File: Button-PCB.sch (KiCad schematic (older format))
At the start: 32 parts

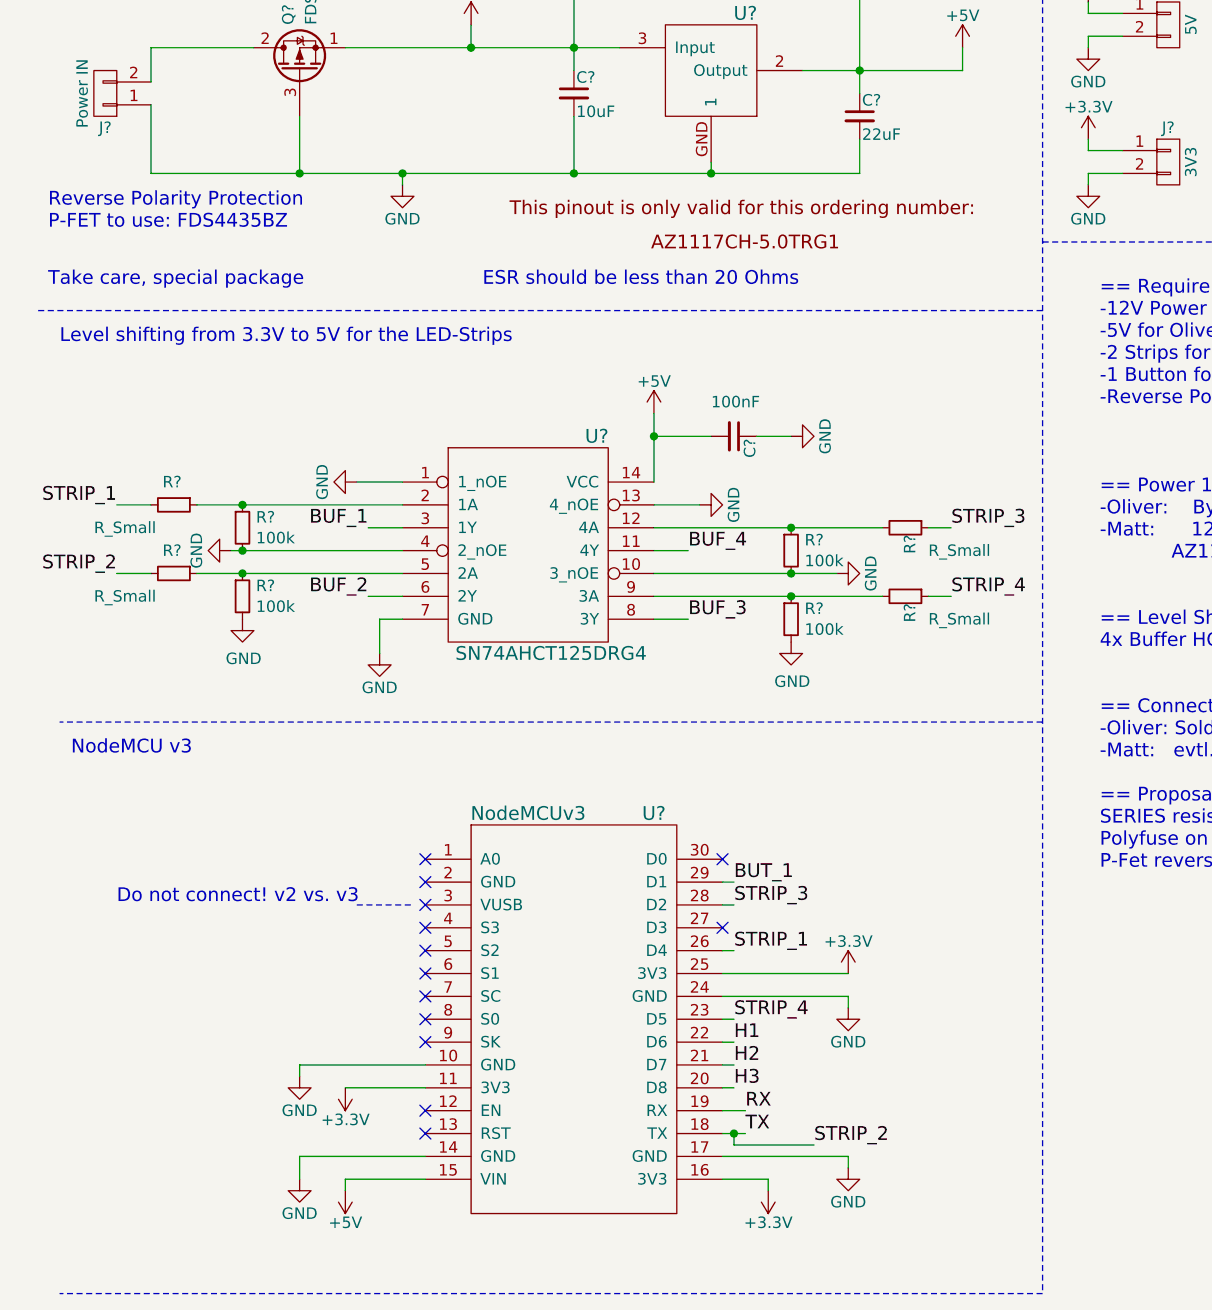
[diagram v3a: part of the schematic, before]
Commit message: Moving series termination resistors from sink (buf) to source (esp)
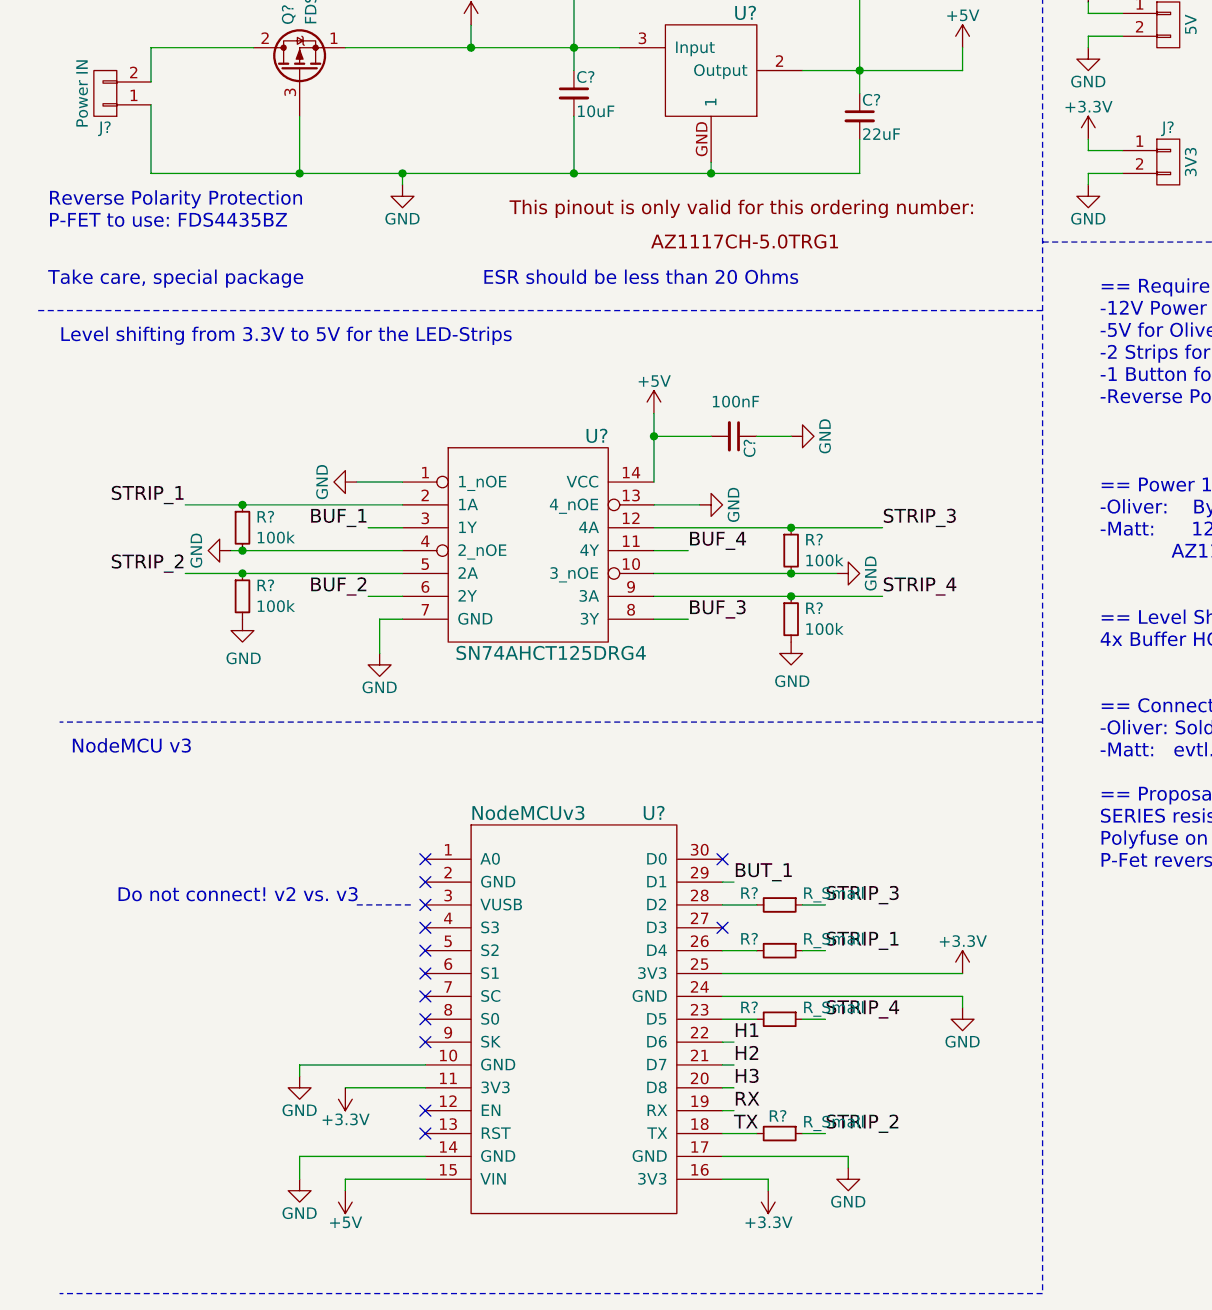
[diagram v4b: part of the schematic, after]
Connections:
- net STRIP_1: now also R?.1, R?.1, U?.2 (1A); no longer R?.2, U?.26 (D4)
- net STRIP_2: now also R?.1, R?.1, U?.5 (2A); no longer J?.1 (P1), R?.2, U?.18 (TX)
- net STRIP_3: now also R?.1, U?.12 (4A); no longer U?.28 (D2)
- net STRIP_4: now also R?.1, U?.9 (3A); no longer U?.23 (D5)
- new net: R?.2, U?.23 (D5)
- new net: R?.2, U?.26 (D4)
- new net: R?.2, U?.28 (D2)
- new net TX: J?.1 (P1), R?.2, U?.18 (TX)
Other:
- moved on the sheet: R?
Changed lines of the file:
@@
 L GND #PWR?
 U 1 1 593F0F99
-P 4050 5850
-F 0 "#PWR?" H 4050 5600 50  0001 C CNN
-F 1 "GND" H 4050 5700 50  0000 C CNN
-F 2 "" H 4050 5850 50  0001 C CNN
-F 3 "" H 4050 5850 50  0001 C CNN
-	1    4050 5850
-	1    0    0    -1
-$EndComp
-Wire Wire Line
-	3500 5800 4050 5800
-Wire Wire Line
-	4050 5800 4050 5850
+P 4550 5850
+F 0 "#PWR?" H 4550 5600 50  0001 C CNN
+F 1 "GND" H 4550 5700 50  0000 C CNN
+F 2 "" H 4550 5850 50  0001 C CNN
+F 3 "" H 4550 5850 50  0001 C CNN
+	1    4550 5850
+	1    0    0    -1
+$EndComp
+Wire Wire Line
+	3500 5800 4550 5800
+Wire Wire Line
+	4550 5800 4550 5850
 Wire Wire Line
 	2200 6100 1650 6100
@@
 L +3.3V #PWR?
 U 1 1 593F1158
-P 4050 5700
-F 0 "#PWR?" H 4050 5550 50  0001 C CNN
-F 1 "+3.3V" H 4050 5840 50  0000 C CNN
-F 2 "" H 4050 5700 50  0001 C CNN
-F 3 "" H 4050 5700 50  0001 C CNN
-	1    4050 5700
+P 4550 5700
+F 0 "#PWR?" H 4550 5550 50  0001 C CNN
+F 1 "+3.3V" H 4550 5840 50  0000 C CNN
+F 2 "" H 4550 5700 50  0001 C CNN
+F 3 "" H 4550 5700 50  0001 C CNN
+	1    4550 5700
 	1    0    0    -1
 $EndComp
@@
 	3700 6600 3700 6650
 Wire Wire Line
-	3500 5700 4050 5700
+	3500 5700 4550 5700
 NoConn ~ 2200 6400
 NoConn ~ 2200 6300
 NoConn ~ 2200 5400
-Text Label 3550 5600 0    60   ~ 0
+Text Label 3950 5600 0    60   ~ 0
 STRIP_1
 Wire Wire Line
-	3500 5600 3550 5600
+	3500 5600 3650 5600
 Text Label 3550 5300 0    60   ~ 0
 BUT_1
 Wire Wire Line
 	3550 5300 3500 5300
-Text Label 3600 6400 0    60   ~ 0
+Text Label 3550 6400 0    60   ~ 0
 TX
-Text Label 3900 6450 0    60   ~ 0
+Text Label 3950 6400 0    60   ~ 0
 STRIP_2
 Wire Wire Line
-	3500 6400 3550 6400
-Wire Wire Line
-	3550 6400 3600 6400
-Wire Wire Line
-	3550 6400 3550 6450
-Wire Wire Line
-	3550 6450 3900 6450
-Connection ~ 3550 6400
-Text Label 3600 6300 0    60   ~ 0
+	3500 6400 3650 6400
+Text Label 3550 6300 0    60   ~ 0
 RX
-Wire Wire Line
-	3500 6300 3600 6300
-Text Label 3550 5400 0    60   ~ 0
+Text Label 3950 5400 0    60   ~ 0
 STRIP_3
-Text Label 3550 5900 0    60   ~ 0
+Text Label 3950 5900 0    60   ~ 0
 STRIP_4
 Wire Wire Line
-	3500 5400 3550 5400
-Wire Wire Line
-	3500 5900 3550 5900
+	3500 5400 3650 5400
+Wire Wire Line
+	3500 5900 3650 5900
 NoConn ~ 2200 5200
 NoConn ~ 2200 5500
@@
 $EndComp
 Wire Wire Line
-	2100 2250 2100 2200
+	2100 2200 2100 2250
 Wire Wire Line
 	4100 2200 4100 2050
 Wire Wire Line
-	3450 2150 3450 2200
+	3450 2200 3450 2150
 Wire Wire Line
 	3850 1750 4100 1750
@@
 	0    -1   -1   0
 $EndComp
-Text Label 850  3950 2    60   ~ 0
+Text Label 1150 3950 2    60   ~ 0
 STRIP_2
-Text Label 850  3650 2    60   ~ 0
+Text Label 1150 3650 2    60   ~ 0
 STRIP_1
-Text Label 4500 3750 0    60   ~ 0
+Text Label 4200 3750 0    60   ~ 0
 STRIP_3
-Text Label 4500 4050 0    60   ~ 0
+Text Label 4200 4050 0    60   ~ 0
 STRIP_4
 $Comp
 L R_Small R?
 U 1 1 5942C75E
-P 1100 3650
-F 0 "R?" V 1000 3600 50  0000 L CNN
-F 1 "R_Small" V 1200 3300 50  0000 L CNN
-F 2 "" H 1100 3650 50  0001 C CNN
-F 3 "" H 1100 3650 50  0001 C CNN
-	1    1100 3650
+P 3750 5600
+F 0 "R?" V 3700 5425 50  0000 L CNN
+F 1 "R_Small" V 3700 5700 50  0000 L CNN
+F 2 "" H 3750 5600 50  0001 C CNN
+F 3 "" H 3750 5600 50  0001 C CNN
+	1    3750 5600
 	0    1    1    0
 $EndComp
@@
 L R_Small R?
 U 1 1 5942CA98
-P 1100 3950
-F 0 "R?" V 1000 3900 50  0000 L CNN
-F 1 "R_Small" V 1200 3600 50  0000 L CNN
-F 2 "" H 1100 3950 50  0001 C CNN
-F 3 "" H 1100 3950 50  0001 C CNN
-	1    1100 3950
+P 3750 6400
+F 0 "R?" V 3675 6350 50  0000 L CNN
+F 1 "R_Small" V 3700 6500 50  0000 L CNN
+F 2 "" H 3750 6400 50  0001 C CNN
+F 3 "" H 3750 6400 50  0001 C CNN
+	1    3750 6400
 	0    1    1    0
 $EndComp
@@
 	1950 3750 2100 3750
 Wire Wire Line
-	1200 3650 1400 3650
+	1150 3650 1400 3650
 Wire Wire Line
 	1400 3650 2100 3650
 Wire Wire Line
-	1200 3950 1400 3950
+	1150 3950 1400 3950
 Wire Wire Line
 	1400 3950 2100 3950
@@
 	1900 3550 2100 3550
 Wire Wire Line
-	4000 3950 3800 3950
-Wire Wire Line
-	3800 3950 3200 3950
+	3200 3950 3800 3950
+Wire Wire Line
+	3800 3950 4000 3950
 Wire Wire Line
 	3400 3650 3200 3650
@@
 L R_Small R?
 U 1 1 5942EF55
-P 4300 3750
-F 0 "R?" H 4330 3770 50  0000 L CNN
-F 1 "R_Small" V 4400 3850 50  0000 L CNN
-F 2 "" H 4300 3750 50  0001 C CNN
-F 3 "" H 4300 3750 50  0001 C CNN
-	1    4300 3750
+P 3750 5400
+F 0 "R?" V 3700 5225 50  0000 L CNN
+F 1 "R_Small" V 3700 5500 50  0000 L CNN
+F 2 "" H 3750 5400 50  0001 C CNN
+F 3 "" H 3750 5400 50  0001 C CNN
+	1    3750 5400
 	0    1    1    0
 $EndComp
@@
 L R_Small R?
 U 1 1 5942F05B
-P 4300 4050
-F 0 "R?" H 4330 4070 50  0000 L CNN
-F 1 "R_Small" V 4400 4150 50  0000 L CNN
-F 2 "" H 4300 4050 50  0001 C CNN
-F 3 "" H 4300 4050 50  0001 C CNN
-	1    4300 4050
+P 3750 5900
+F 0 "R?" V 3700 5725 50  0000 L CNN
+F 1 "R_Small" V 3700 6000 50  0000 L CNN
+F 2 "" H 3750 5900 50  0001 C CNN
+F 3 "" H 3750 5900 50  0001 C CNN
+	1    3750 5900
 	0    1    1    0
 $EndComp
@@
 Wire Wire Line
 	3800 4050 4200 4050
-Wire Wire Line
-	4400 3750 4500 3750
-Wire Wire Line
-	4500 4050 4400 4050
 $Comp
 L C_Small C?
@@
 Wire Notes Line
 	4900 7100 600  7100
-Wire Wire Line
-	1000 3650 850  3650
-Wire Wire Line
-	1000 3950 850  3950
 $Comp
 L R_Small R?
@@
 $EndComp
 Connection ~ 3800 3950
+Wire Wire Line
+	3950 5600 3850 5600
+Wire Wire Line
+	3850 5900 3950 5900
+Wire Wire Line
+	3550 6300 3500 6300
+Wire Wire Line
+	3850 6400 3950 6400
+Wire Wire Line
+	3950 5400 3850 5400
 $EndSCHEMATC

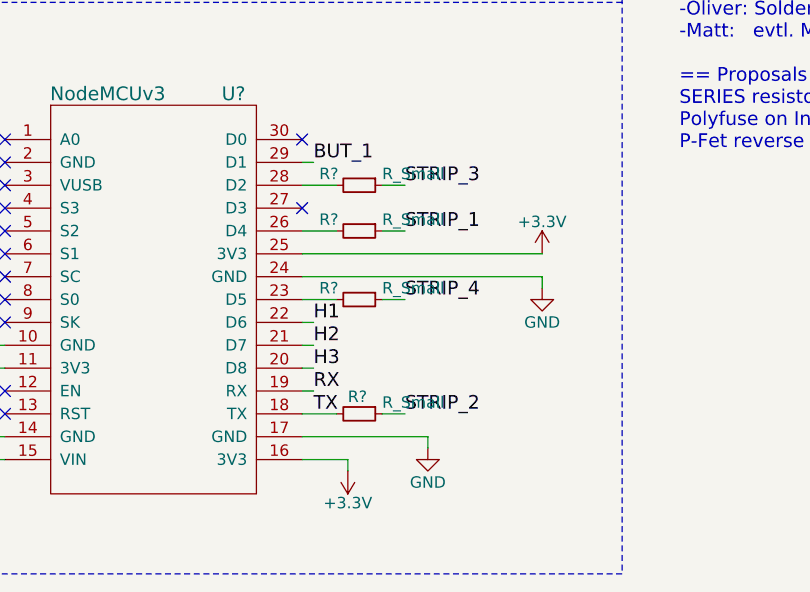
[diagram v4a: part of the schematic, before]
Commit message: Value of series termination resistors: 100R
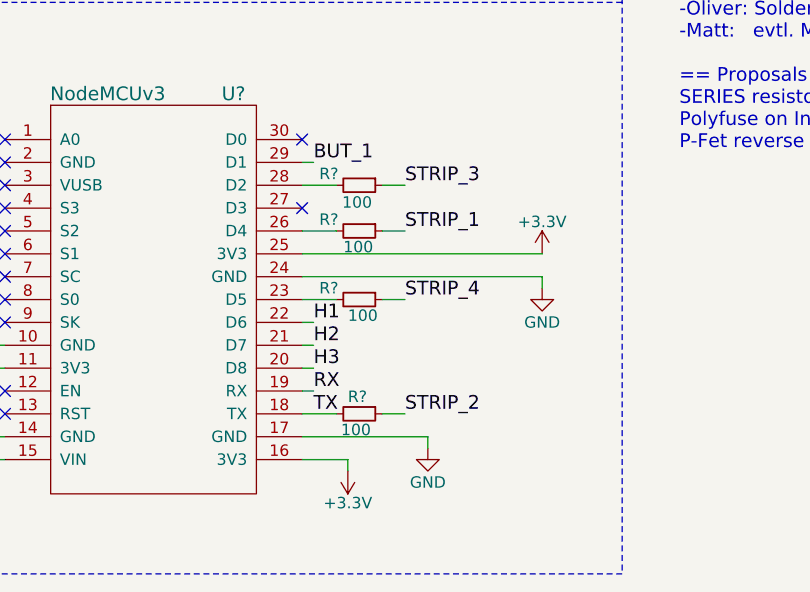
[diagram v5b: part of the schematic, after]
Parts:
- R? (x4): value R_Small -> 100
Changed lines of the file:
@@
 P 3750 5600
 F 0 "R?" V 3700 5425 50  0000 L CNN
-F 1 "R_Small" V 3700 5700 50  0000 L CNN
+F 1 "100" V 3820 5530 50  0000 L CNN
 F 2 "" H 3750 5600 50  0001 C CNN
 F 3 "" H 3750 5600 50  0001 C CNN
@@
 P 3750 6400
 F 0 "R?" V 3675 6350 50  0000 L CNN
-F 1 "R_Small" V 3700 6500 50  0000 L CNN
+F 1 "100" V 3820 6320 50  0000 L CNN
 F 2 "" H 3750 6400 50  0001 C CNN
 F 3 "" H 3750 6400 50  0001 C CNN
@@
 P 3750 5400
 F 0 "R?" V 3700 5225 50  0000 L CNN
-F 1 "R_Small" V 3700 5500 50  0000 L CNN
+F 1 "100" V 3825 5325 50  0000 L CNN
 F 2 "" H 3750 5400 50  0001 C CNN
 F 3 "" H 3750 5400 50  0001 C CNN
@@
 P 3750 5900
 F 0 "R?" V 3700 5725 50  0000 L CNN
-F 1 "R_Small" V 3700 6000 50  0000 L CNN
+F 1 "100" V 3820 5850 50  0000 L CNN
 F 2 "" H 3750 5900 50  0001 C CNN
 F 3 "" H 3750 5900 50  0001 C CNN

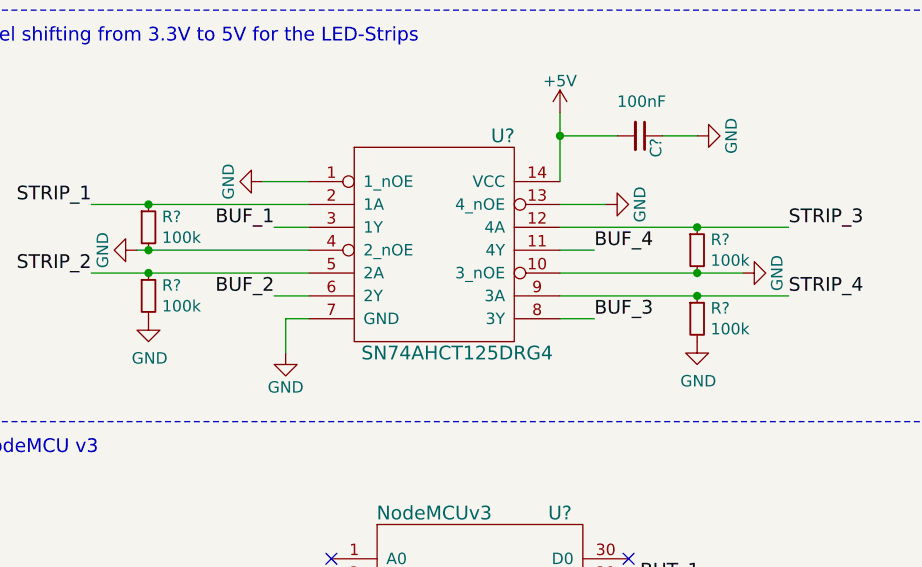
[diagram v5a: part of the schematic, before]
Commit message: Reducing pull-down resistor values from 100k to 10k
A 10k resistor is already used as pull-up for the button. This change
keeps the number of distinct resistor values low.
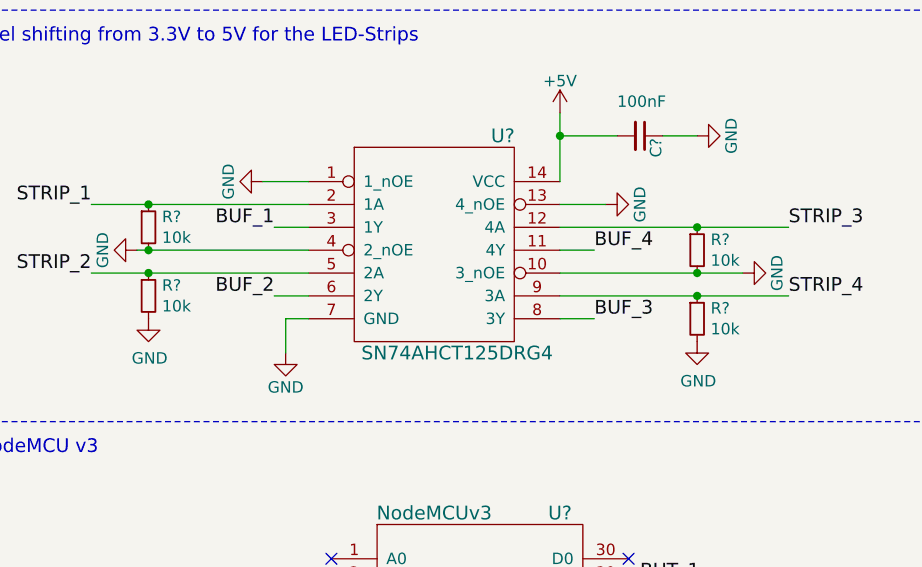
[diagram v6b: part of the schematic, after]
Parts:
- R? (x4): value 100k -> 10k
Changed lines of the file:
@@
 P 1400 4050
 F 0 "R?" H 1459 4096 50  0000 L CNN
-F 1 "100k" H 1459 4005 50  0000 L CNN
+F 1 "10k" H 1459 4005 50  0000 L CNN
 F 2 "" H 1400 4050 50  0001 C CNN
 F 3 "" H 1400 4050 50  0001 C CNN
@@
 P 1400 3750
 F 0 "R?" H 1459 3796 50  0000 L CNN
-F 1 "100k" H 1459 3705 50  0000 L CNN
+F 1 "10k" H 1459 3705 50  0000 L CNN
 F 2 "" H 1400 3750 50  0001 C CNN
 F 3 "" H 1400 3750 50  0001 C CNN
@@
 P 3800 3850
 F 0 "R?" H 3859 3896 50  0000 L CNN
-F 1 "100k" H 3859 3805 50  0000 L CNN
+F 1 "10k" H 3859 3805 50  0000 L CNN
 F 2 "" H 3800 3850 50  0001 C CNN
 F 3 "" H 3800 3850 50  0001 C CNN
@@
 P 3800 4150
 F 0 "R?" H 3859 4196 50  0000 L CNN
-F 1 "100k" H 3859 4105 50  0000 L CNN
+F 1 "10k" H 3859 4105 50  0000 L CNN
 F 2 "" H 3800 4150 50  0001 C CNN
 F 3 "" H 3800 4150 50  0001 C CNN
